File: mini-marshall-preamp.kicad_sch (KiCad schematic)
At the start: 37 parts, among them J1 LO, J2 HI, J3 AudioJack2, J4 6V3, J6 370V, U1 6N2P, U2 6N2P

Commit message: Fixed the schematic
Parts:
- added R15: 100k 2W, symbol Device:R
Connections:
- net at R9.1, U1.1 (A): now also C6.2
- net at C14.1, R12.2, R13.1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: no longer C6.2
- net at C2.2, U1.6 (A): now also R15.2; no longer C13.1, R12.1
- new net: C13.1, R12.1, R15.1
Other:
- moved on the sheet: C6, R9
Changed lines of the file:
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@@
 	)
 	(junction
-		(at 185.42 151.13)
+		(at 121.92 60.96)
 		(diameter 0)
 		(color 0 0 0 0)
 	)
 	(junction
-		(at 204.47 87.63)
+		(at 185.42 151.13)
 		(diameter 0)
 		(color 0 0 0 0)
 	)
 	(junction
-		(at 100.33 63.5)
+		(at 204.47 87.63)
 		(diameter 0)
 		(color 0 0 0 0)
 	)
 	(junction
-		(at 73.66 62.23)
+		(at 100.33 63.5)
 		(diameter 0)
 		(color 0 0 0 0)
@@
 	)
 	(junction
-		(at 142.24 34.29)
+		(at 212.09 151.13)
 		(diameter 0)
 		(color 0 0 0 0)
 	)
 	(junction
-		(at 212.09 151.13)
+		(at 142.24 60.96)
 		(diameter 0)
 		(color 0 0 0 0)
@@
 	)
 	(junction
-		(at 238.76 102.87)
+		(at 73.66 62.23)
 		(diameter 0)
 		(color 0 0 0 0)
 	)
 	(junction
-		(at 142.24 60.96)
+		(at 238.76 102.87)
 		(diameter 0)
 		(color 0 0 0 0)
@@
 	(wire
 		(pts
+			(xy 135.89 60.96) (xy 142.24 60.96)
+		)
+		(stroke
+			(width 0)
+			(type default)
+		)
+	)
+	(wire
+		(pts
 			(xy 223.52 83.82) (xy 218.44 83.82)
 		)
@@
 	(wire
 		(pts
-			(xy 121.92 58.42) (xy 121.92 64.77)
+			(xy 121.92 58.42) (xy 121.92 60.96)
 		)
 		(stroke
@@
 	(wire
 		(pts
-			(xy 142.24 58.42) (xy 142.24 60.96)
-		)
-		(stroke
-			(width 0)
-			(type default)
-		)
-	)
-	(wire
-		(pts
-			(xy 142.24 34.29) (xy 167.64 34.29)
+			(xy 121.92 34.29) (xy 167.64 34.29)
 		)
 		(stroke
@@
 	(wire
 		(pts
+			(xy 121.92 60.96) (xy 121.92 64.77)
+		)
+		(stroke
+			(width 0)
+			(type default)
+		)
+	)
+	(wire
+		(pts
 			(xy 218.44 123.19) (xy 223.52 123.19)
 		)
@@
 	(wire
 		(pts
+			(xy 121.92 60.96) (xy 128.27 60.96)
+		)
+		(stroke
+			(width 0)
+			(type default)
+		)
+	)
+	(wire
+		(pts
 			(xy 261.62 104.14) (xy 259.08 104.14)
 		)
@@
 	(wire
 		(pts
+			(xy 73.66 34.29) (xy 73.66 49.53)
+		)
+		(stroke
+			(width 0)
+			(type default)
+		)
+	)
+	(wire
+		(pts
 			(xy 45.72 74.93) (xy 45.72 81.28)
 		)
@@
 	(wire
 		(pts
-			(xy 73.66 62.23) (xy 73.66 34.29)
-		)
-		(stroke
-			(width 0)
-			(type default)
-		)
-	)
-	(wire
-		(pts
 			(xy 30.48 74.93) (xy 45.72 74.93)
 		)
@@
 	(wire
 		(pts
-			(xy 142.24 34.29) (xy 142.24 50.8)
-		)
-		(stroke
-			(width 0)
-			(type default)
-		)
-	)
-	(wire
-		(pts
 			(xy 100.33 63.5) (xy 100.33 71.12)
 		)
@@
 	(wire
 		(pts
-			(xy 121.92 34.29) (xy 142.24 34.29)
+			(xy 73.66 57.15) (xy 73.66 62.23)
 		)
 		(stroke
@@
 	(symbol
 		(lib_id "Device:R")
-		(at 121.92 54.61 180)
+		(at 121.92 54.61 0)
+		(mirror x)
 		(unit 1)
 		(exclude_from_sim no)
@@
 		(on_board yes)
 		(dnp no)
-		(fields_autoplaced yes)
 		(property "Reference" "R9"
-			(at 124.46 53.3399 0)
+			(at 119.38 53.3399 0)
 			(effects
 				(font
@@
 		)
 		(property "Value" "100k 1W"
-			(at 124.46 55.8799 0)
+			(at 119.38 55.8799 0)
 			(effects
 				(font
@@
 		)
 		(property "Footprint" ""
-			(at 123.698 54.61 90)
+			(at 120.142 54.61 90)
 			(effects
 				(font
@@
 	(symbol
 		(lib_id "Device:C")
-		(at 142.24 54.61 180)
+		(at 132.08 60.96 270)
 		(unit 1)
 		(exclude_from_sim no)
@@
 		(on_board yes)
 		(dnp no)
-		(fields_autoplaced yes)
 		(property "Reference" "C6"
-			(at 146.05 53.3399 0)
+			(at 132.08 53.34 90)
 			(effects
 				(font
 					(size 1.27 1.27)
 				)
-				(justify right)
 			)
 		)
 		(property "Value" "22n 450v"
-			(at 146.05 55.8799 0)
+			(at 132.08 55.88 90)
 			(effects
 				(font
 					(size 1.27 1.27)
 				)
-				(justify right)
 			)
 		)
 		(property "Footprint" ""
-			(at 141.2748 50.8 0)
+			(at 128.27 61.9252 0)
 			(effects
 				(font
@@
 		)
 		(property "Datasheet" "~"
-			(at 142.24 54.61 0)
+			(at 132.08 60.96 0)
 			(effects
 				(font
@@
 		)
 		(property "Description" "Unpolarized capacitor"
-			(at 142.24 54.61 0)
+			(at 132.08 60.96 0)
 			(effects
 				(font
@@
 					(unit 1)
 				)
+			)
+		)
+	)
+	(symbol
+		(lib_id "Device:R")
+		(at 73.66 53.34 0)
+		(mirror y)
+		(unit 1)
+		(exclude_from_sim no)
+		(in_bom yes)
+		(on_board yes)
+		(dnp no)
+		(property "Reference" "R15"
+			(at 71.12 52.0699 0)
+			(effects
+				(font
+					(size 1.27 1.27)
+				)
+				(justify left)
+			)
+		)
+		(property "Value" "100k 2W"
+			(at 71.12 54.6099 0)
+			(effects
+				(font
+					(size 1.27 1.27)
+				)
+				(justify left)
+			)
+		)
+		(property "Footprint" ""
+			(at 75.438 53.34 90)
+			(effects
+				(font
+					(size 1.27 1.27)
+				)
+				(hide yes)
+			)
+		)
+		(property "Datasheet" "~"
+			(at 73.66 53.34 0)
+			(effects
+				(font
+					(size 1.27 1.27)
+				)
+				(hide yes)
+			)
+		)
+		(property "Description" "Resistor"
+			(at 73.66 53.34 0)
+			(effects
+				(font
+					(size 1.27 1.27)
+				)
+				(hide yes)
+			)
+		)
+		(pin "1"
+		)
+		(pin "2"
+		)
+		(instances
+			(project ""
+				(path "/91d70738-8a39-4af9-b6d6-ee03b177697f"
+					(reference "R15")
+					(unit 1)
+				)

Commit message: Swap units A & B of the tubes for consistency
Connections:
- net at C5.1, R6.1, R7.1: now also U2.2 (G); no longer U2.7 (G)
- net at C6.2, R9.1: now also U1.6 (A); no longer U1.1 (A)
- net at C14.1, R12.2, R13.1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: now also U2.6 (A); no longer U2.1 (A)
- net at C9.2, R10.2, R11.1: now also U2.8 (K); no longer U2.3 (K)
- net at R5.1: now also U1.8 (K); no longer U1.3 (K)
- net at C2.2, R15.2: now also U1.1 (A); no longer U1.6 (A)
- net at C4.2, RV1.2: now also U1.7 (G); no longer U1.2 (G)
- net at R2.2: now also U1.2 (G); no longer U1.7 (G)
- net at C12.1, R3.2: now also U1.3 (K); no longer U1.8 (K)
- net at R8.2: now also U2.3 (K); no longer U2.8 (K)
- new net: R14.1, U2.1 (A), U2.7 (G)
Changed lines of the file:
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@@
 		(lib_id "tubes:6N2P")
 		(at 207.01 74.93 0)
-		(unit 2)
+		(unit 1)
 		(exclude_from_sim no)
 		(in_bom yes)
@@
 				(path "/91d70738-8a39-4af9-b6d6-ee03b177697f"
 					(reference "U2")
-					(unit 2)
+					(unit 1)
 				)
 			)
@@
 		(lib_id "tubes:6N2P")
 		(at 73.66 74.93 0)
-		(unit 1)
+		(unit 2)
 		(exclude_from_sim no)
 		(in_bom yes)
@@
 				(path "/91d70738-8a39-4af9-b6d6-ee03b177697f"
 					(reference "U1")
-					(unit 1)
+					(unit 2)
 				)
 			)
@@
 		(lib_id "tubes:6N2P")
 		(at 121.92 74.93 0)
-		(unit 2)
+		(unit 1)
 		(exclude_from_sim no)
 		(in_bom yes)
@@
 				(path "/91d70738-8a39-4af9-b6d6-ee03b177697f"
 					(reference "U1")
-					(unit 2)
+					(unit 1)
 				)
 			)
@@
 		(lib_id "tubes:6N2P")
 		(at 167.64 74.93 0)
-		(unit 1)
+		(unit 2)
 		(exclude_from_sim no)
 		(in_bom yes)
@@
 				(path "/91d70738-8a39-4af9-b6d6-ee03b177697f"
 					(reference "U2")
-					(unit 1)
-				)
-			)
+					(unit 2)
+				)
+			)

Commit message: Update schematic with extra caps and proper input jacks
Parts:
- removed J1: LO, symbol Connector_Audio:AudioJack2
- removed J2: HI, symbol Connector_Audio:AudioJack2
- added C1, C7: 20u 450V, symbol Device:C_Polarized
- added J1: LO, symbol Connector_Audio:AudioJack2_Switch
- added J2: HI, symbol Connector_Audio:AudioJack2_Switch
- added R16, R17: 4.7k 2W, symbol Device:R
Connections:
- net GND: now also C1.2, C7.2, J1.T, J1.TN, J2.T, J2.TN
- net at C14.1, R13.1, U2.6 (A): now also R16.2; no longer R12.2, R14.2, R9.2
- net at R1.1, R2.1: now also J2.S, J2.SN
- net at C2.1: now also J1.SN
- net at C3.1, R4.2: now also J1.S
- new net: C7.1, R12.2, R17.1, R9.2
- new net: C1.1, R14.2, R16.1, R17.2

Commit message: Start PCB
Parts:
- added J5: 370V GND, Connector_Wire:SolderWire-1.5sqmm_1x01_D1.7mm_OD3.9mm, symbol Connector:Screw_Terminal_01x01
- added J7: 6V3 GND, Connector_Wire:SolderWire-1.5sqmm_1x01_D1.7mm_OD3.9mm, symbol Connector:Screw_Terminal_01x01
- C1, C13, C14, C7: footprint (none) -> Capacitor_THT:CP_Radial_D13.0mm_P7.50mm
- C10, C11, C9: footprint (none) -> Capacitor_THT:C_Rect_L9.0mm_W2.5mm_P7.50mm_MKT
- C12: footprint (none) -> Capacitor_THT:C_Rect_L9.0mm_W4.2mm_P7.50mm_MKT
- C2: footprint (none) -> Capacitor_THT:C_Rect_L11.5mm_W5.1mm_P10.00mm_MKT
- C3, C4, C5: footprint (none) -> Capacitor_THT:C_Rect_L7.0mm_W2.5mm_P5.00mm
- C6: footprint (none) -> Capacitor_THT:C_Rect_L11.5mm_W5.0mm_P10.00mm_MKT
- J1, J2, J3: footprint (none) -> Connector_Audio:Jack_6.35mm_Neutrik_NMJ6HFD2-AU_Horizontal
- J4, J6: footprint (none) -> Connector_Wire:SolderWire-1.5sqmm_1x01_D1.7mm_OD3.9mm
- R1, R10, R2, R3, R5, R6, R7, R8: footprint (none) -> Resistor_THT:R_Axial_DIN0207_L6.3mm_D2.5mm_P10.16mm_Horizontal
- R11, R12, R13, R14, R15, R16, R17, R4, R9: footprint (none) -> Resistor_THT:R_Axial_DIN0516_L15.5mm_D5.0mm_P20.32mm_Horizontal
- RV1, RV2, RV3, RV4, RV5: footprint (none) -> Potentiometer_THT:Potentiometer_Alps_RK163_Single_Horizontal
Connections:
- net GND: now also J5.1 (Pin_1), J7.1 (Pin_1)

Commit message: Use external connection footprints for pots and jacks
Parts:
- J1: footprint Connector_Audio:Jack_6.35mm_Neutrik_NMJ6HFD2-AU_Horizontal -> Connector_Wire:SolderWire-1sqmm_1x04_P5.4mm_D1.4mm_OD2.7mm
- J2: footprint Connector_Audio:Jack_6.35mm_Neutrik_NMJ6HFD2-AU_Horizontal -> Connector_Wire:SolderWire-1sqmm_1x02_P5.4mm_D1.4mm_OD2.7mm
- J3: value AudioJack2 -> OUT; footprint Connector_Audio:Jack_6.35mm_Neutrik_NMJ6HFD2-AU_Horizontal -> Connector_Wire:SolderWire-1sqmm_1x02_P5.4mm_D1.4mm_OD2.7mm
- RV1, RV2, RV3, RV4, RV5: footprint Potentiometer_THT:Potentiometer_Alps_RK163_Single_Horizontal -> Connector_Wire:SolderWire-1sqmm_1x03_P5.4mm_D1.4mm_OD2.7mm
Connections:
- net GND: now also J1.3 (T), J1.4 (TN), J2.3 (T), J2.4 (TN), J3.2 (T); no longer J1.T, J1.TN, J2.T, J2.TN, J3.T
- net at C2.1: now also J1.2 (SN); no longer J1.SN
- net at R1.1, R2.1: now also J2.1 (S), J2.2 (SN); no longer J2.S, J2.SN
- net at C3.1, R4.2: now also J1.1 (S); no longer J1.S
- net at RV5.2: now also J3.1 (S); no longer J3.S
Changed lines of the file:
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@@
 			)
 		)
-		(property "Footprint" "Potentiometer_THT:Potentiometer_Alps_RK163_Single_Horizontal"
+		(property "Footprint" "Connector_Wire:SolderWire-1sqmm_1x03_P5.4mm_D1.4mm_OD2.7mm"
 			(at 238.76 95.25 0)
 			(effects
@@
 			)
 		)
-		(property "Footprint" "Potentiometer_THT:Potentiometer_Alps_RK163_Single_Horizontal"
+		(property "Footprint" "Connector_Wire:SolderWire-1sqmm_1x03_P5.4mm_D1.4mm_OD2.7mm"
 			(at 100.33 74.93 0)
 			(effects
@@
 			)
 		)
-		(property "Footprint" "Connector_Audio:Jack_6.35mm_Neutrik_NMJ6HFD2-AU_Horizontal"
+		(property "Footprint" "Connector_Wire:SolderWire-1sqmm_1x02_P5.4mm_D1.4mm_OD2.7mm"
 			(at 21.59 74.93 0)
 			(effects
@@
 			)
 		)
-		(pin "SN"
+		(pin "3"
 		)
-		(pin "S"
+		(pin "1"
 		)
-		(pin "TN"
+		(pin "4"
 		)
-		(pin "T"
+		(pin "2"
 		)
 		(instances
@@
 			)
 		)
-		(property "Value" "AudioJack2"
+		(property "Value" "OUT"
 			(at 271.78 104.7749 0)
 			(effects
@@
 			)
 		)
-		(property "Footprint" "Connector_Audio:Jack_6.35mm_Neutrik_NMJ6HFD2-AU_Horizontal"
+		(property "Footprint" "Connector_Wire:SolderWire-1sqmm_1x02_P5.4mm_D1.4mm_OD2.7mm"
 			(at 266.7 104.14 0)
 			(effects
@@
 			)
 		)
-		(pin "T"
+		(pin "1"
 		)
-		(pin "S"
+		(pin "2"
 		)
 		(instances
@@
 			)
 		)
-		(property "Footprint" "Potentiometer_THT:Potentiometer_Alps_RK163_Single_Horizontal"
+		(property "Footprint" "Connector_Wire:SolderWire-1sqmm_1x03_P5.4mm_D1.4mm_OD2.7mm"
 			(at 238.76 109.22 0)
 			(effects
@@
 			)
 		)
-		(property "Footprint" "Potentiometer_THT:Potentiometer_Alps_RK163_Single_Horizontal"
+		(property "Footprint" "Connector_Wire:SolderWire-1sqmm_1x03_P5.4mm_D1.4mm_OD2.7mm"
 			(at 238.76 123.19 0)
 			(effects
@@
 			)
 		)
-		(property "Footprint" "Potentiometer_THT:Potentiometer_Alps_RK163_Single_Horizontal"
+		(property "Footprint" "Connector_Wire:SolderWire-1sqmm_1x03_P5.4mm_D1.4mm_OD2.7mm"
 			(at 252.73 101.6 0)
 			(effects
@@
 	)
 	(symbol
+		(lib_name "AudioJack2_Switch_1")
 		(lib_id "Connector_Audio:AudioJack2_Switch")
 		(at 21.59 64.77 0)
@@
 			)
 		)
-		(property "Footprint" "Connector_Audio:Jack_6.35mm_Neutrik_NMJ6HFD2-AU_Horizontal"
+		(property "Footprint" "Connector_Wire:SolderWire-1sqmm_1x04_P5.4mm_D1.4mm_OD2.7mm"
 			(at 21.59 59.69 0)
 			(effects
@@
 			)
 		)
-		(pin "SN"
+		(pin "1"
 		)
-		(pin "S"
+		(pin "2"
 		)
-		(pin "TN"
+		(pin "4"
 		)
-		(pin "T"
+		(pin "3"
 		)
 		(instances

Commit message: First PCB layout
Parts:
- removed J2: HI, Connector_Wire:SolderWire-1sqmm_1x02_P5.4mm_D1.4mm_OD2.7mm, symbol Connector_Audio:AudioJack2_Switch
- added J2: HI, Connector_Wire:SolderWire-1sqmm_1x02_P5.4mm_D1.4mm_OD2.7mm, symbol Connector_Audio:AudioJack2
- R4: footprint Resistor_THT:R_Axial_DIN0516_L15.5mm_D5.0mm_P20.32mm_Horizontal -> Resistor_THT:R_Axial_DIN0207_L6.3mm_D2.5mm_P10.16mm_Horizontal
- U1, U2: footprint Valve:Valve_Noval_P -> tubes:Valve_6N2P-3
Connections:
- net GND: now also J2.2 (T)
- net at R1.1, R2.1: now also J2.1 (S)
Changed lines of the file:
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@@
 	)
 	(junction
-		(at 26.67 74.93)
-		(diameter 0)
-		(color 0 0 0 0)
-	)
-	(junction
 		(at 26.67 64.77)
 		(diameter 0)
@@
 	)
 	(junction
-		(at 26.67 80.01)
-		(diameter 0)
-		(color 0 0 0 0)
-	)
-	(junction
 		(at 142.24 60.96)
 		(diameter 0)
@@
 	(wire
 		(pts
-			(xy 31.75 80.01) (xy 31.75 82.55)
+			(xy 31.75 77.47) (xy 31.75 80.01)
 		)
 		(stroke
@@
 	(wire
 		(pts
-			(xy 26.67 80.01) (xy 26.67 82.55)
-		)
-		(stroke
-			(width 0)
-			(type default)
-		)
-	)
-	(wire
-		(pts
 			(xy 97.79 121.92) (xy 97.79 125.73)
 		)
@@
 	(wire
 		(pts
-			(xy 26.67 80.01) (xy 31.75 80.01)
+			(xy 26.67 77.47) (xy 31.75 77.47)
 		)
 		(stroke
@@
 	(wire
 		(pts
-			(xy 26.67 74.93) (xy 26.67 77.47)
-		)
-		(stroke
-			(width 0)
-			(type default)
-		)
-	)
-	(wire
-		(pts
 			(xy 73.66 34.29) (xy 73.66 49.53)
 		)
@@
 			)
 		)
-		(property "Footprint" "Valve:Valve_Noval_P"
+		(property "Footprint" "tubes:Valve_6N2P-3"
 			(at 104.648 147.32 0)
 			(effects
@@
 	)
 	(symbol
-		(lib_id "Connector_Audio:AudioJack2_Switch")
-		(at 21.59 80.01 0)
-		(unit 1)
-		(exclude_from_sim no)
-		(in_bom yes)
-		(on_board yes)
-		(dnp no)
-		(property "Reference" "J2"
-			(at 21.59 85.344 0)
-			(effects
-				(font
-					(size 1.27 1.27)
-				)
-			)
-		)
-		(property "Value" "HI"
-			(at 21.59 87.376 0)
-			(effects
-				(font
-					(size 1.27 1.27)
-				)
-			)
-		)
-		(property "Footprint" "Connector_Wire:SolderWire-1sqmm_1x02_P5.4mm_D1.4mm_OD2.7mm"
-			(at 21.59 74.93 0)
-			(effects
-				(font
-					(size 1.27 1.27)
-				)
-				(hide yes)
-			)
-		)
-		(property "Datasheet" "~"
-			(at 21.59 74.93 0)
-			(effects
-				(font
-					(size 1.27 1.27)
-				)
-				(hide yes)
-			)
-		)
-		(property "Description" "Audio Jack, 2 Poles (Mono / TS), Switched Pole (Normalling)"
-			(at 21.59 80.01 0)
-			(effects
-				(font
-					(size 1.27 1.27)
-				)
-				(hide yes)
-			)
-		)
-		(pin "3"
-		)
-		(pin "1"
-		)
-		(pin "4"
-		)
-		(pin "2"
-		)
-		(instances
-			(project ""
-				(path "/91d70738-8a39-4af9-b6d6-ee03b177697f"
-					(reference "J2")
-					(unit 1)
-				)
-			)
-		)
-	)
-	(symbol
 		(lib_id "power:GND")
 		(at 82.55 48.26 0)
@@
 			)
 		)
-		(property "Footprint" "Valve:Valve_Noval_P"
+		(property "Footprint" "tubes:Valve_6N2P-3"
 			(at 213.868 85.09 0)
 			(effects
@@
 			)
 		)
-		(property "Footprint" "Valve:Valve_Noval_P"
+		(property "Footprint" "tubes:Valve_6N2P-3"
 			(at 194.818 147.32 0)
 			(effects
@@
 			)
 		)
-		(property "Footprint" "Valve:Valve_Noval_P"
+		(property "Footprint" "tubes:Valve_6N2P-3"
 			(at 80.518 85.09 0)
 			(effects
@@
 			)
 		)
-		(property "Footprint" "Resistor_THT:R_Axial_DIN0516_L15.5mm_D5.0mm_P20.32mm_Horizontal"
+		(property "Footprint" "Resistor_THT:R_Axial_DIN0207_L6.3mm_D2.5mm_P10.16mm_Horizontal"
 			(at 93.98 65.278 90)
 			(effects
@@
 	(symbol
 		(lib_id "power:GND")
-		(at 31.75 82.55 0)
+		(at 31.75 80.01 0)
 		(unit 1)
 		(exclude_from_sim no)
@@
 		(fields_autoplaced yes)
 		(property "Reference" "#PWR017"
-			(at 31.75 88.9 0)
+			(at 31.75 86.36 0)
 			(effects
 				(font
@@
 		)
 		(property "Value" "GND"
-			(at 31.75 87.63 0)
+			(at 31.75 85.09 0)
 			(effects
 				(font
@@
 		)
 		(property "Footprint" ""
-			(at 31.75 82.55 0)
+			(at 31.75 80.01 0)
 			(effects
 				(font
@@
 		)
 		(property "Datasheet" ""
-			(at 31.75 82.55 0)
+			(at 31.75 80.01 0)
 			(effects
 				(font
@@
 		)
 		(property "Description" "Power symbol creates a global label with name \"GND\" , ground"
-			(at 31.75 82.55 0)
+			(at 31.75 80.01 0)
 			(effects
 				(font
@@
 			)
 		)
-		(property "Footprint" "Valve:Valve_Noval_P"
+		(property "Footprint" "tubes:Valve_6N2P-3"
 			(at 128.778 85.09 0)
 			(effects
@@
 			)
 		)
-		(property "Footprint" "Valve:Valve_Noval_P"
+		(property "Footprint" "tubes:Valve_6N2P-3"
 			(at 174.498 85.09 0)
 			(effects
@@
 					(unit 1)
 				)
+			)
+		)
+	)
+	(symbol
+		(lib_id "Connector_Audio:AudioJack2")
+		(at 21.59 77.47 0)
+		(unit 1)
+		(exclude_from_sim no)
+		(in_bom yes)
+		(on_board yes)
+		(dnp no)
+		(property "Reference" "J2"
+			(at 16.51 75.5649 0)
+			(effects
+				(font
+					(size 1.27 1.27)
+				)
+				(justify right)
+			)
+		)
+		(property "Value" "HI"
+			(at 16.51 78.1049 0)
+			(effects
+				(font
+					(size 1.27 1.27)
+				)
+				(justify right)
+			)
+		)
+		(property "Footprint" "Connector_Wire:SolderWire-1sqmm_1x02_P5.4mm_D1.4mm_OD2.7mm"
+			(at 21.59 77.47 0)
+			(effects
+				(font
+					(size 1.27 1.27)
+				)
+				(hide yes)
+			)
+		)
+		(property "Datasheet" "~"
+			(at 21.59 77.47 0)
+			(effects
+				(font
+					(size 1.27 1.27)
+				)
+				(hide yes)
+			)
+		)
+		(property "Description" "Audio Jack, 2 Poles (Mono / TS)"
+			(at 21.59 77.47 0)
+			(effects
+				(font
+					(size 1.27 1.27)
+				)
+				(hide yes)
+			)
+		)
+		(pin "1"
+		)
+		(pin "2"
+		)
+		(instances
+			(project "mini-marshall-preamp"
+				(path "/91d70738-8a39-4af9-b6d6-ee03b177697f"
+					(reference "J2")
+					(unit 1)
+				)

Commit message: Layout attempt
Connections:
- net GND: no longer J7.1 (Pin_1), U1.5 (H1), U2.5 (H1)
- net at C5.1, R6.1, R7.1: now also U2.7 (G); no longer U2.2 (G)
- net at C6.2, R9.1: now also U1.1 (A); no longer U1.6 (A)
- net at C9.2, R10.2, R11.1: now also U2.3 (K); no longer U2.8 (K)
- net at R5.1: now also U1.3 (K); no longer U1.8 (K)
- net at C2.2, R15.2: now also U1.6 (A); no longer U1.1 (A)
- net at C4.2, RV1.2: now also U1.2 (G); no longer U1.7 (G)
- net at C14.1, R13.1, R16.2: now also U2.1 (A); no longer U2.6 (A)
- net at R2.2: now also U1.7 (G); no longer U1.2 (G)
- net at C12.1, R3.2: now also U1.8 (K); no longer U1.3 (K)
- net at R8.2: now also U2.8 (K); no longer U2.3 (K)
- new net: R14.1, U2.2 (G), U2.6 (A)
- new net GND1: J7.1 (Pin_1), U1.5 (H1), U2.5 (H1)

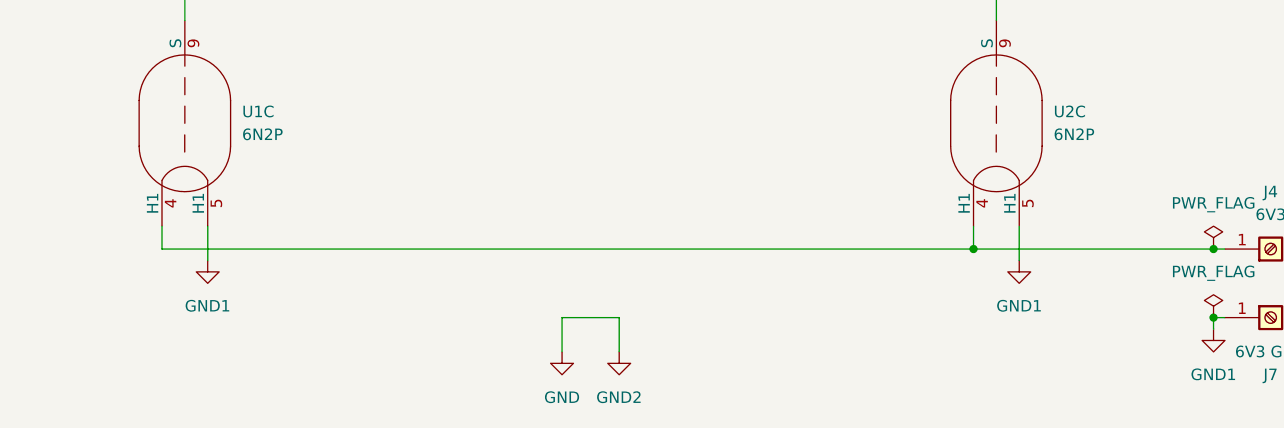
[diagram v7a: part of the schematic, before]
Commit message: Restart laying out board for size optimization
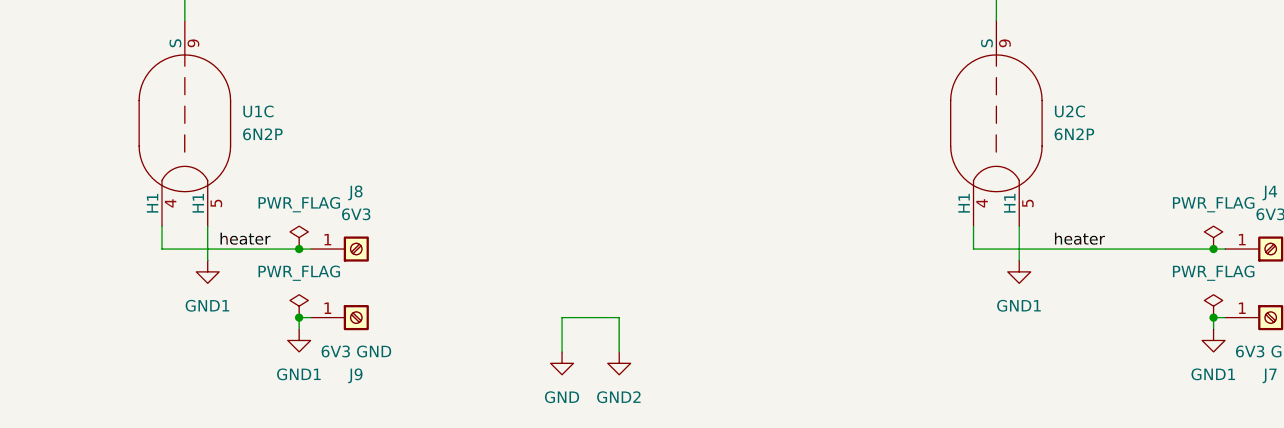
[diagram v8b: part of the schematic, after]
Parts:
- added J8: 6V3, Connector_Wire:SolderWire-1.5sqmm_1x01_D1.7mm_OD3.9mm, symbol Connector:Screw_Terminal_01x01
- added J9: 6V3 GND, Connector_Wire:SolderWire-1.5sqmm_1x01_D1.7mm_OD3.9mm, symbol Connector:Screw_Terminal_01x01
- J1: footprint Connector_Wire:SolderWire-1sqmm_1x04_P5.4mm_D1.4mm_OD2.7mm -> Connector_Wire:SolderWire-1sqmm_1x03_P7.8mm_D1.4mm_OD3.9mm
- J2, J3: footprint Connector_Wire:SolderWire-1sqmm_1x02_P5.4mm_D1.4mm_OD2.7mm -> Connector_Wire:SolderWire-1sqmm_1x02_P7.8mm_D1.4mm_OD3.9mm
- RV1, RV2, RV3, RV4, RV5: footprint Connector_Wire:SolderWire-1sqmm_1x03_P5.4mm_D1.4mm_OD2.7mm -> Connector_Wire:SolderWire-1sqmm_1x03_P7.8mm_D1.4mm_OD3.9mm
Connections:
- net GND1: now also J9.1 (Pin_1)
- net heater: now reaches J4.1 (Pin_1), U1.4 (H1), U2.4 (H1)
- net heater: now also J8.1 (Pin_1)
